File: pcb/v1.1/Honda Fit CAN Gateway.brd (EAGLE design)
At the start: 53.3 x 30.5 mm, 19 parts, among them Q1 10MHz, U1 TEENSY_3.1_BASIC, U2 MCP2515TSOP, U3 TJA1050, U4 TJA1050, X1 CON_10X2F_JAE_MX34020NF1

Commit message: V1.1 PCB preliminary commit
Need to review.  All signals routed - no rats.
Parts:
- removed C2: (no value), resistor:C0603
- removed PAD1, PAD2, PAD3, PAD4: (no value), wirepad:3,17/1,3
- removed Q1: 10MHz, crystal:HC49/S
- added JP1: (no value), pinhead:1X04
- added R10, R11, R5, R6, R7: 0R, resistor:R0805
- added R12, R8, R9: 10k, resistor:R0805
- added U5: CB3, ductapemaster_custom:4-SMD
- C1: value (none) -> 100n
- moved C1 11.0 mm to (46.2, 19.6), flipped to the bottom, turned to 270 degrees
- moved C3 10.5 mm to (28.9, 23.3), flipped to the bottom, turned to 180 degrees
- moved U2 5.59 mm to (30.5, 18.8), flipped to the bottom, turned to 270 degrees
- moved R1 0.72 mm to (39.9, 5.21)
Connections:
- new net !RESET: R8.1, U1.5, U2.19
- new net CLK_10MHZ: U2.9, U5.P$3
- new net N$6: R5.1, U2.17
- new net N$7: R6.1, U2.16
- new net N$8: R7.1, U2.14
- new net N$9: C3.1, R12.2, U2.20
- net !HUCAN: now also JP1.4; no longer PAD2.1
- net +5V: now also C1.1, R12.1, R8.2, U5.P$1, U5.P$4; no longer C3.1, U2.19, U2.20
- net GND: now also R9.1, U5.P$2; no longer C2.2
- net HFL: now also JP1.1, R10.1; no longer PAD4.1, U1.23/A9
- net HUCAN: now also JP1.3; no longer PAD1.1
- net MISO: now also R5.2; no longer U2.17
- net MOSI: now also R6.2; no longer U2.16
- net N$1: now also R9.2; no longer C1.1, Q1.2
- net N$2: now also R10.2, U1.22/A8; no longer C2.1, Q1.1, U2.9
- net N$3: now also R11.2, U1.23/A9; no longer U1.5
- net PARK_SW: now also JP1.2, R11.1; no longer PAD3.1, U1.22/A8
- net SCK: now also R7.2; no longer U2.14
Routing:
- net +5V: track 2.00 -> 15.9 mm, vias 0 -> 3
- net !RESET: track 0.00 -> 11.9 mm
- net !HUCAN: track 7.61 -> 15.9 mm
- net HUCAN: track 7.88 -> 15.8 mm
- net N$1: track 10.9 -> 3.16 mm
- net N$3: track 0.00 -> 6.92 mm, vias 0 -> 1
- net CLK_10MHZ: track 0.00 -> 6.69 mm
- net HUCAN_TX: track 11.2 -> 17.7 mm, vias 0 -> 1
- net BCAN_RX: track 31.5 -> 25.7 mm, vias 1 -> 0
- net N$2: track 8.05 -> 2.35 mm
- net PARK_SW: track 49.1 -> 44.1 mm, vias 1 -> 0
- net !INT: track 7.99 -> 12.5 mm, vias 0 -> 1
- net GND: track 14.9 -> 10.5 mm, vias 8 -> 5
- net N$8: track 0.00 -> 4.23 mm
- net BCAN_TX: track 34.6 -> 30.9 mm, vias 1 -> 0
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
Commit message: Change resistor value
Change resistor land used for MCP2515 supply inductor to be 0 ohms for clarity
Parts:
- R12: value 10k -> 0R
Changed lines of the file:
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@@
 <attribute name="NAME" x="44.45" y="3.683" size="0.8128" layer="26" rot="MR90"/>
 </element>
-<element name="R12" library="resistor" package="R0805" value="10k" x="25.4" y="23.368" smashed="yes" rot="MR180"/>
+<element name="R12" library="resistor" package="R0805" value="0R" x="25.4" y="23.368" smashed="yes" rot="MR180"/>
 </elements>
 <signals>

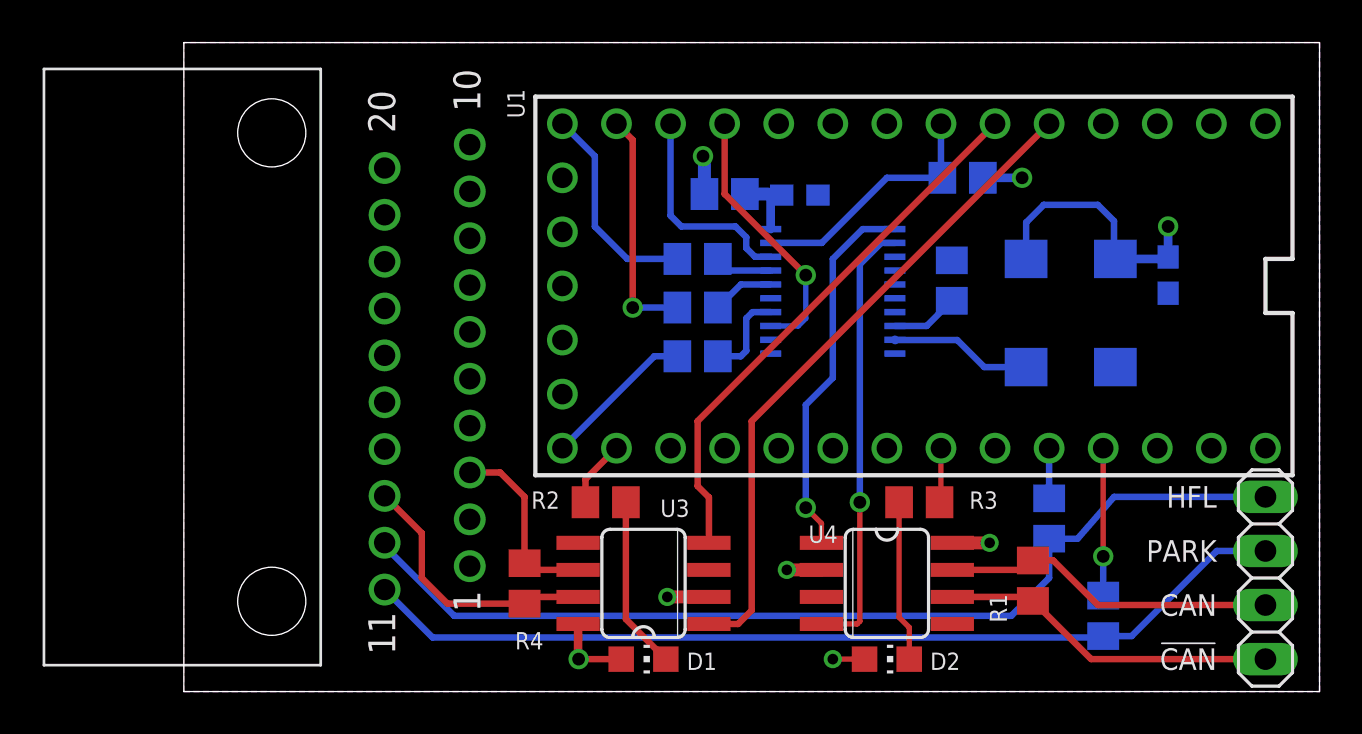
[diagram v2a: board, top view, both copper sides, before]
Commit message: Move silkscreen and a couple of traces
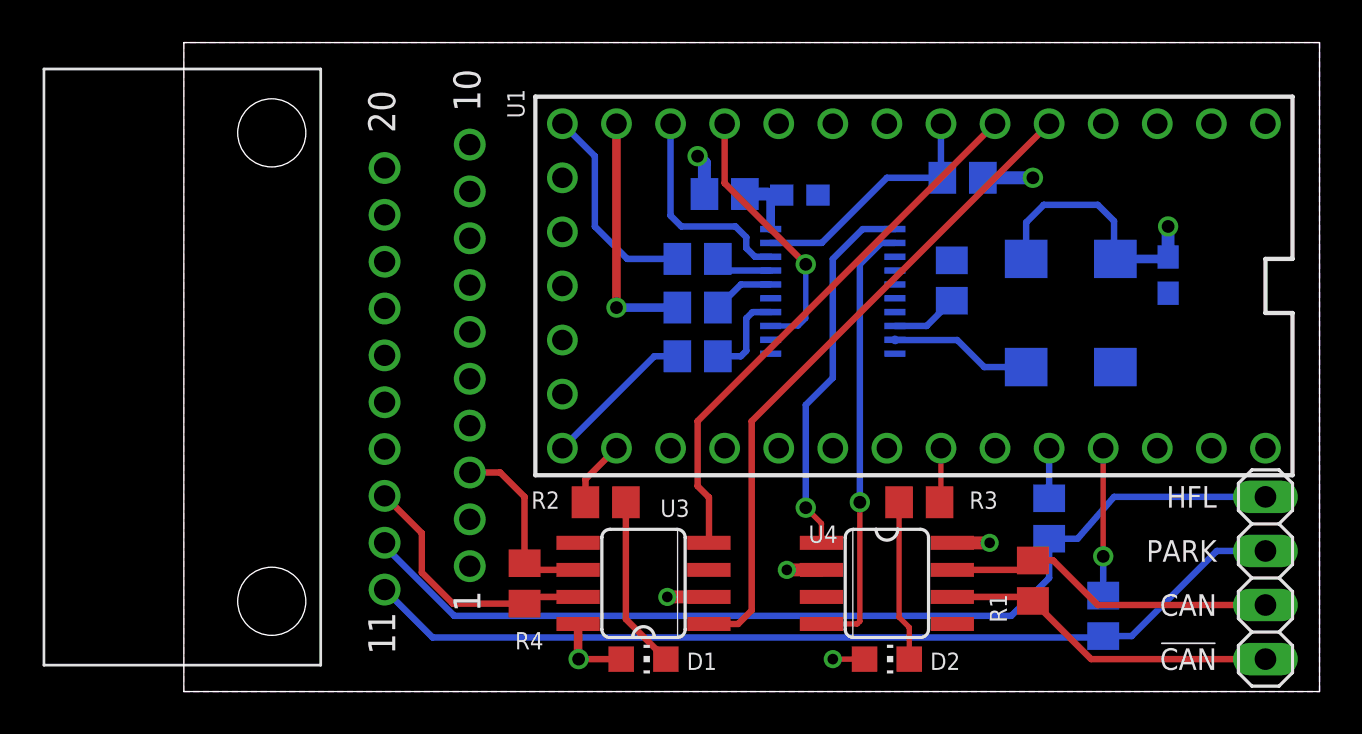
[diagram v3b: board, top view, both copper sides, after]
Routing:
- net +5V: track 15.9 -> 16.5 mm
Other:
- board text added: "Dan Kouba, 2017"
- board text added: "PCB v1.1"
- board text removed: "Dan Kouba, 2015"
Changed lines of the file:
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@@
 <text x="48.514" y="1.016" size="1.016" layer="25" align="bottom-right">!CAN</text>
 <text x="48.514" y="7.112" size="1.016" layer="25" rot="R180">PARK</text>
-<text x="38.1" y="31.242" size="1.27" layer="26" font="vector" rot="MR0" align="center">Honda Fit CAN Gateway</text>
-<text x="37.846" y="29.718" size="1.27" layer="26" font="vector" rot="MR0" align="center">Dan Kouba, 2015</text>
+<text x="7.366" y="15.748" size="1.27" layer="26" font="vector" rot="MR90" align="center">Honda Fit CAN Gateway</text>
+<text x="5.334" y="15.494" size="1.27" layer="26" font="vector" rot="MR270" align="center">Dan Kouba, 2017</text>
 <text x="27.686" y="29.21" size="1.27" layer="26" font="vector" rot="MR0" align="center">https://github.com/Ductapemaster/HondaFitHDMI</text>
+<text x="3.556" y="15.494" size="1.27" layer="26" font="vector" rot="MR270" align="center">PCB v1.1</text>
 </plain>
 <attributes>
@@
 <contactref element="U1" pad="11"/>
 <contactref element="R6" pad="2"/>
-<wire x1="20.32" y1="26.67" x2="21.082" y2="25.908" width="0.3048" layer="1"/>
-<wire x1="21.082" y1="25.908" x2="21.082" y2="18.034" width="0.3048" layer="1"/>
-<via x="21.082" y="18.034" extent="1-16" drill="0.6"/>
-<wire x1="21.082" y1="18.034" x2="23.18" y2="18.034" width="0.3048" layer="16"/>
+<wire x1="23.18" y1="18.034" x2="20.32" y2="18.034" width="0.4064" layer="16"/>
+<via x="20.32" y="18.034" extent="1-16" drill="0.6"/>
+<wire x1="20.32" y1="18.034" x2="20.32" y2="26.67" width="0.4064" layer="1"/>
 </signal>
 <signal name="BCAN_RX">
@@
 <contactref element="U2" pad="13"/>
 <contactref element="U1" pad="9"/>
-<wire x1="25.4" y1="26.67" x2="25.4" y2="23.368" width="0.3048" layer="1"/>
-<wire x1="25.4" y1="23.368" x2="29.21" y2="19.558" width="0.3048" layer="1"/>
-<via x="29.21" y="19.558" extent="1-16" drill="0.6"/>
-<wire x1="29.21" y1="19.558" x2="29.21" y2="17.526" width="0.254" layer="16"/>
+<wire x1="25.4" y1="26.67" x2="25.4" y2="23.876" width="0.3048" layer="1"/>
+<wire x1="25.4" y1="23.876" x2="29.21" y2="20.066" width="0.3048" layer="1"/>
+<via x="29.21" y="20.066" extent="1-16" drill="0.6"/>
+<wire x1="29.21" y1="20.066" x2="29.21" y2="17.526" width="0.254" layer="16"/>
 <wire x1="29.21" y1="17.526" x2="28.855" y2="17.171" width="0.254" layer="16"/>
 <wire x1="27.5622" y1="17.171" x2="28.855" y2="17.171" width="0.254" layer="16"/>
@@
 <contactref element="U5" pad="P$4"/>
 <contactref element="U5" pad="P$1"/>
-<wire x1="46.228" y1="20.408" x2="46.228" y2="21.844" width="0.4064" layer="16"/>
+<wire x1="46.228" y1="20.408" x2="46.228" y2="21.844" width="0.6096" layer="16"/>
 <via x="46.228" y="21.844" extent="1-16" drill="0.6"/>
 <wire x1="43.7515" y1="20.32" x2="46.14" y2="20.32" width="0.4064" layer="16"/>
@@
 <wire x1="43.688" y1="22.098" x2="43.688" y2="20.3835" width="0.3048" layer="16"/>
 <wire x1="43.688" y1="20.3835" x2="43.7515" y2="20.32" width="0.4064" layer="16"/>
-<wire x1="37.526" y1="24.13" x2="39.37" y2="24.13" width="0.4064" layer="16"/>
-<via x="39.37" y="24.13" extent="1-16" drill="0.6"/>
+<wire x1="37.526" y1="24.13" x2="39.878" y2="24.13" width="0.6096" layer="16"/>
+<via x="39.878" y="24.13" extent="1-16" drill="0.6"/>
 <contactref element="R12" pad="1"/>
-<wire x1="24.45" y1="23.368" x2="24.45" y2="25.08" width="0.6096" layer="16"/>
-<wire x1="24.45" y1="25.08" x2="24.384" y2="25.146" width="0.6096" layer="16"/>
-<via x="24.384" y="25.146" extent="1-16" drill="0.6"/>
+<wire x1="24.45" y1="23.368" x2="24.45" y2="24.826" width="0.6096" layer="16"/>
+<wire x1="24.45" y1="24.826" x2="24.13" y2="25.146" width="0.6096" layer="16"/>
+<via x="24.13" y="25.146" extent="1-16" drill="0.6"/>
 </signal>
 <signal name="HUCAN_RX">
@@
 <contactref element="X1" pad="P13"/>
 <contactref element="U3" pad="7"/>
-<wire x1="11.176" y1="5.334" x2="12.38" y2="4.13" width="0.3048" layer="1"/>
-<wire x1="11.176" y1="5.334" x2="11.176" y2="7.444" width="0.3048" layer="1"/>
+<wire x1="11.176" y1="5.588" x2="12.634" y2="4.13" width="0.3048" layer="1"/>
+<wire x1="11.176" y1="5.588" x2="11.176" y2="7.444" width="0.3048" layer="1"/>
 <wire x1="11.176" y1="7.444" x2="9.43" y2="9.19" width="0.3048" layer="1"/>
 <contactref element="R4" pad="1"/>
 <wire x1="18.5166" y1="4.445" x2="16.317" y2="4.445" width="0.3048" layer="1"/>
 <wire x1="16.317" y1="4.445" x2="16.002" y2="4.13" width="0.254" layer="1"/>
-<wire x1="16.002" y1="4.13" x2="12.38" y2="4.13" width="0.3048" layer="1"/>
+<wire x1="16.002" y1="4.13" x2="12.634" y2="4.13" width="0.3048" layer="1"/>
 </signal>
 <signal name="!BCAN">
